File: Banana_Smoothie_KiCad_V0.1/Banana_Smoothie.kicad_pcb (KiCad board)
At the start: 2 copper layers, 100 x 80 mm, 128 parts, among them IC1 LPC1769, IC5 LD117ADT33TR, Q1 BSL207SP, Q2 12MHz, SW1 SW_TACT_4P_B, SW3 SW_TACT_4P_B, U3 USD-SOCKETUSD, X14 USB

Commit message: Added LAN8720_Module
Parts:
- removed C26, C27: 220u, E2,5-7
- removed C28: .1uF, C0603
- removed D2: 214AC, DO-214AC
- removed IC2: ~, TO263-5
- removed L2: 33uH, CDRH125
- removed R16, R28, R29, R31, R4: 1K, R0603
- added M1: LM2596_Module, Banana_Smoothie_Footprints:LM2596_Module, F.Cu at (156.7, 90.2)
- JP1: footprint 2X07%2f90 -> Banana_Smoothie_Footprints:LAN8720_Module; moved to F.Cu
- moved JP1 20.6 mm to (159.1, 160.2), turned to 90 degrees
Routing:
- net GND: track 830.1 -> 694.2 mm, vias 68 -> 44
- net +3V3: track 540.1 -> 476.2 mm, vias 22 -> 19
- net /RTS: track 106.0 -> 56.2 mm, vias 5 -> 1
- net /ESPTX: track 68.8 -> 22.8 mm, vias 4 -> 1
- net 5vreg: track 74.9 -> 30.7 mm, vias 1 -> 0
- net /ESPRX: track 65.4 -> 21.3 mm, vias 4 -> 1
- net /N$18: track 30.0 -> 0.00 mm, vias 2 -> 0
- net /N$9: track 29.7 -> 0.00 mm
- net /RESET1: track 24.9 -> 0.00 mm
- net /24V: track 131.3 -> 110.2 mm
- net /2: track 17.6 -> 0.00 mm, vias 2 -> 0
- net /15: track 15.4 -> 0.00 mm, vias 2 -> 0
- net /ISP_BOOT: track 60.3 -> 46.6 mm, vias 4 -> 3
- net /12: track 5.12 -> 0.00 mm
- net /RESET: track 98.9 -> 95.5 mm
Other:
- board text removed: "HC-06"

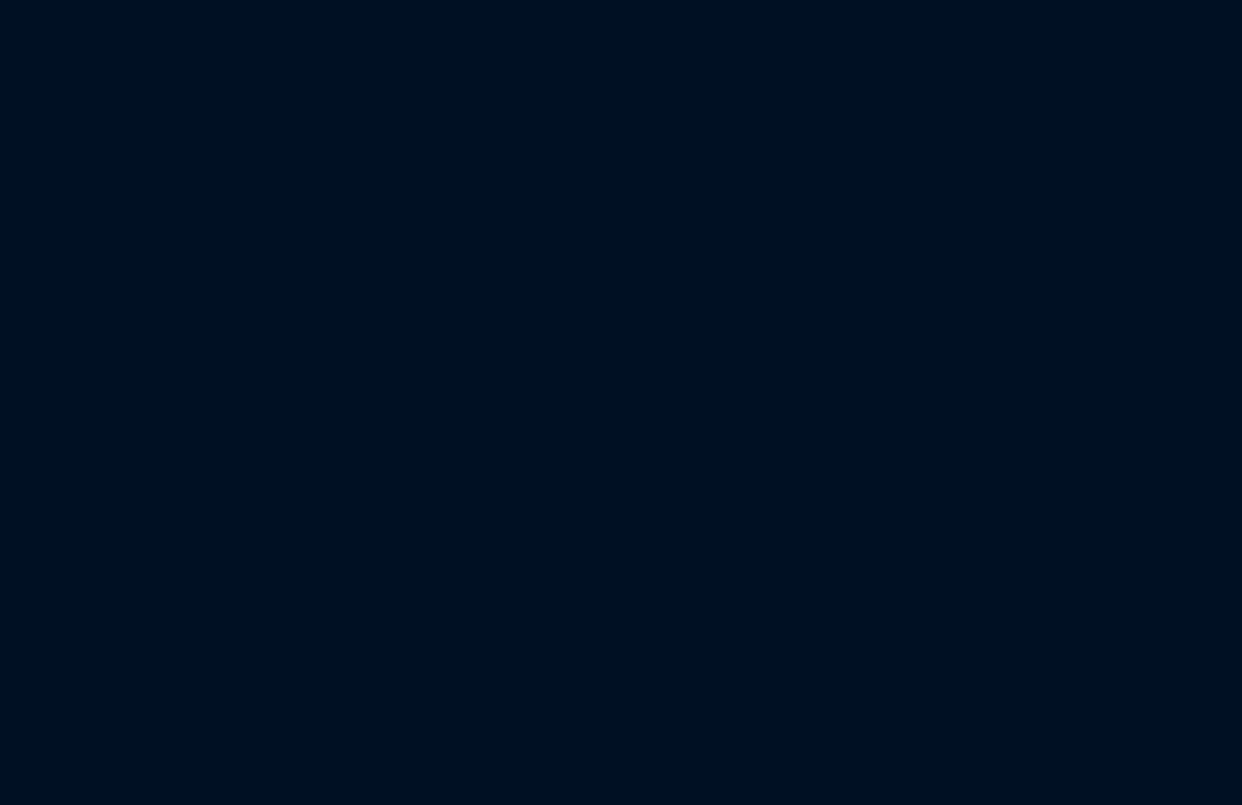
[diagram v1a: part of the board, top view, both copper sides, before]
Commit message: Added reverse polarity protection
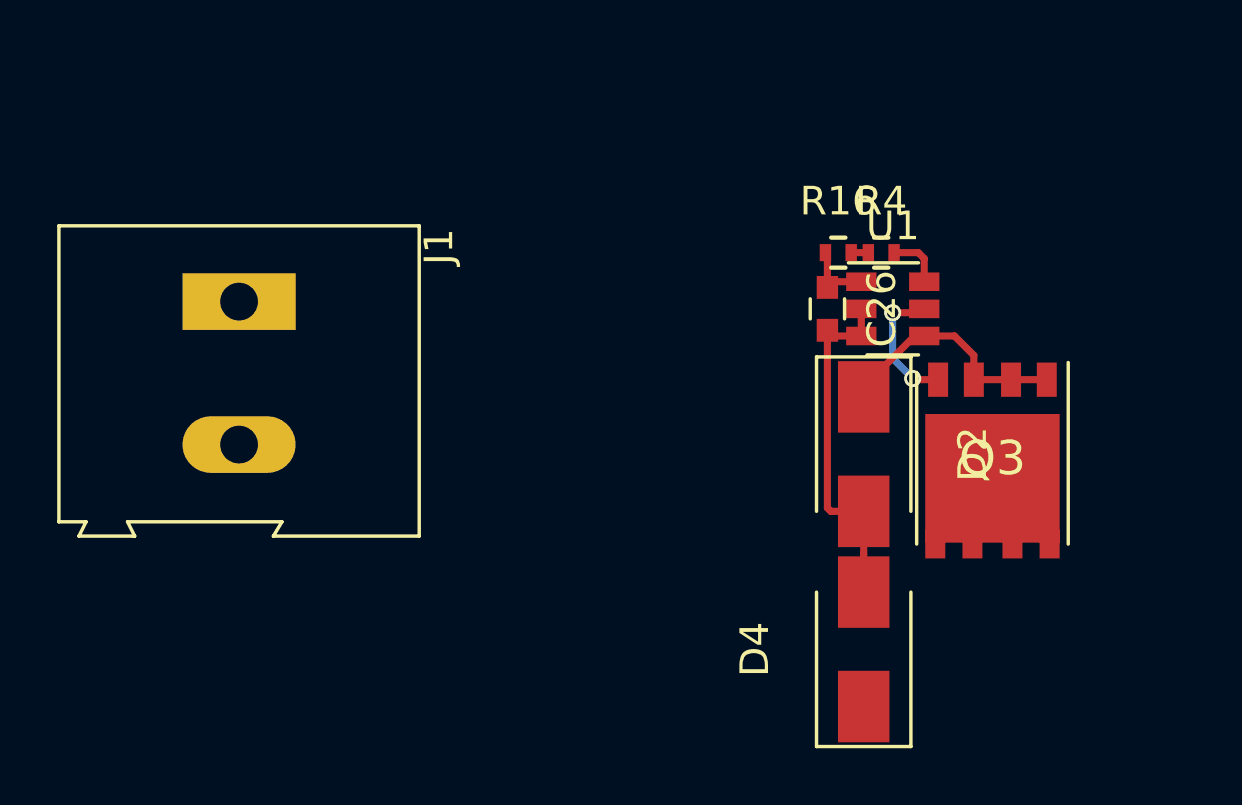
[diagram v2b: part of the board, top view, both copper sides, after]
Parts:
- added C26: 100n, Capacitors_SMD:C_0603, F.Cu at (80.5, 159.8)
- added D2: SS16, Diodes_SMD:D_SMA_Standard, F.Cu at (81.8, 164.8)
- added D4: SS16, Diodes_SMD:D_SMA_Standard, F.Cu at (81.8, 171.7)
- added J1: Screw_Terminal_1x02, Connect:AK300-2, F.Cu at (59.9, 159.5)
- added Q3: Q_NMOS_DSG, Banana_Smoothie_Footprints:PG-TDSON-8, F.Cu at (86.3, 165.0)
- added R16: 47R, Resistors_SMD:R_0402, F.Cu at (80.9, 157.8)
- added R4: 47R, Resistors_SMD:R_0402, F.Cu at (82.4, 157.8)
- added U1: LM5050, TO_SOT_Packages_SMD:SOT-23-6, F.Cu at (82.8, 159.8)
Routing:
- net GND: track 694.2 -> 991.2 mm, vias 44 -> 45
- net /PWM1_BED_HEATER: track 63.1 -> 9.57 mm
- net /PWM0_PSU_OUT: track 60.7 -> 8.57 mm
- net /STP5: track 56.9 -> 13.3 mm, vias 2 -> 1
- net /BUZZER-RRD: track 47.7 -> 6.30 mm
- net /P1_30_CLICK-ON-RRD: track 43.7 -> 7.38 mm
- net /P2.6_FAN_FET: track 65.4 -> 30.4 mm
- net /P2.7_HOTEND_FET: track 67.5 -> 32.6 mm
- net 5vreg: track 30.7 -> 44.7 mm
- net /X_MIN: track 44.5 -> 30.4 mm
- net Net-(C26-Pad2): track 0.00 -> 12.6 mm
- net Net-(D2-Pad1): track 0.00 -> 8.62 mm
- net Net-(Q3-PadG): track 0.00 -> 4.66 mm, vias 0 -> 2
- net Net-(C26-Pad1): track 0.00 -> 2.51 mm
- net /24V: track 110.2 -> 112.2 mm
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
